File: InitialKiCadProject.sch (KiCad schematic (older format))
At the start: 0 parts

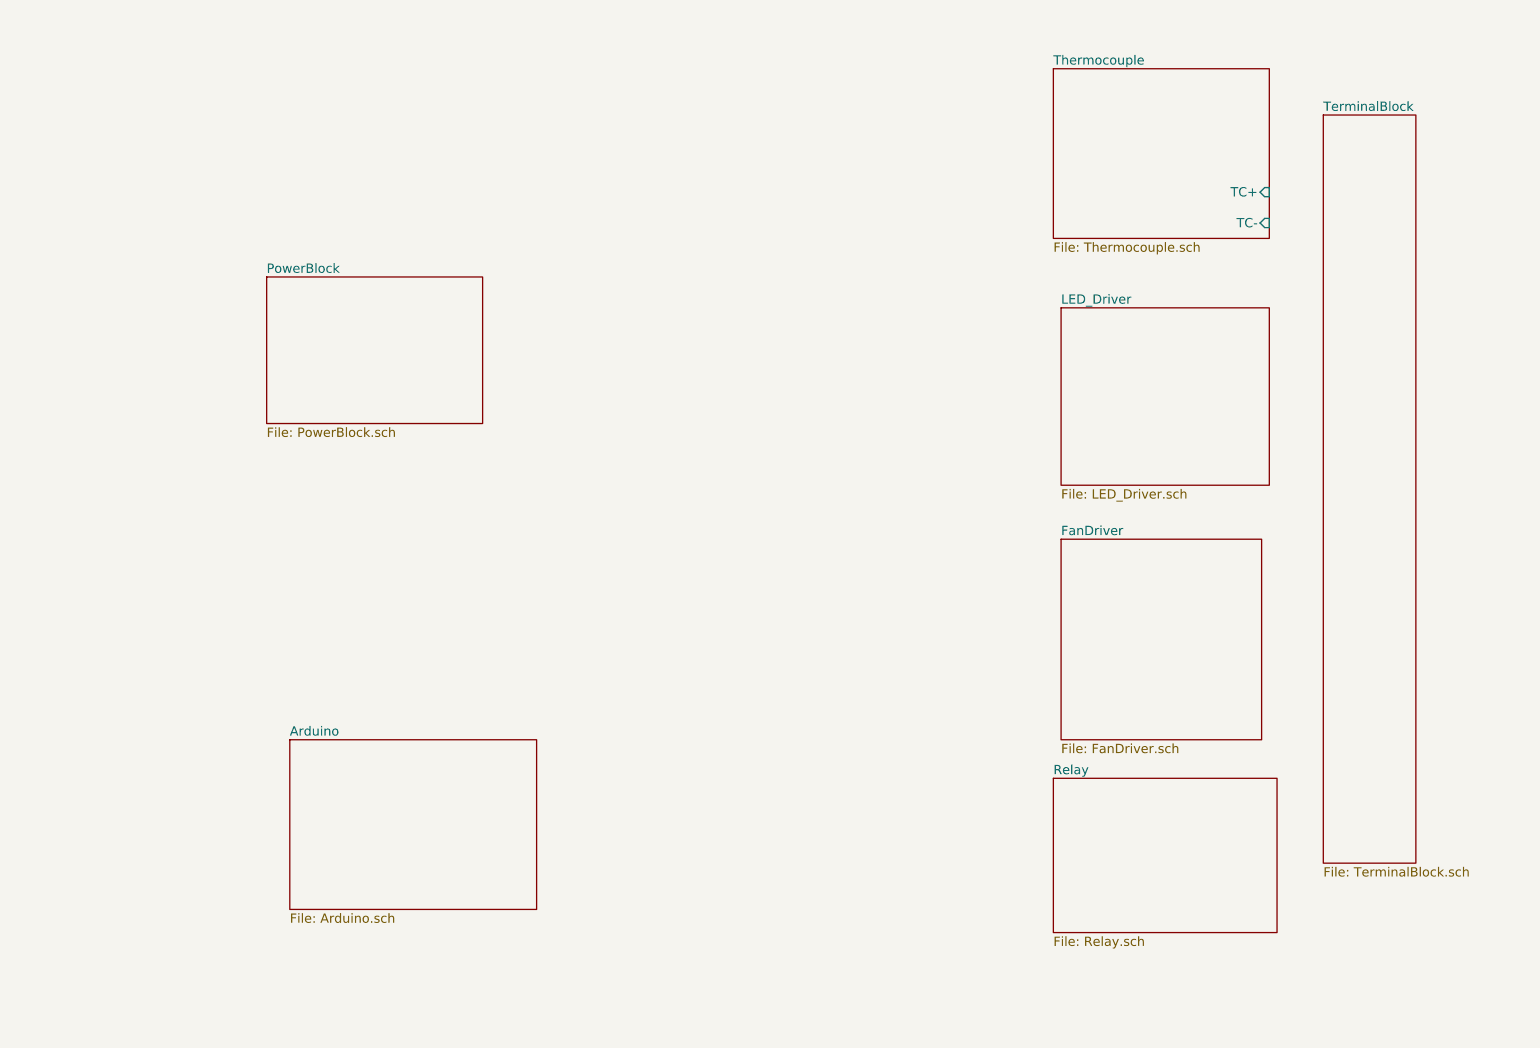
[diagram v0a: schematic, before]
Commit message: Added pins to sheets of block diagram.
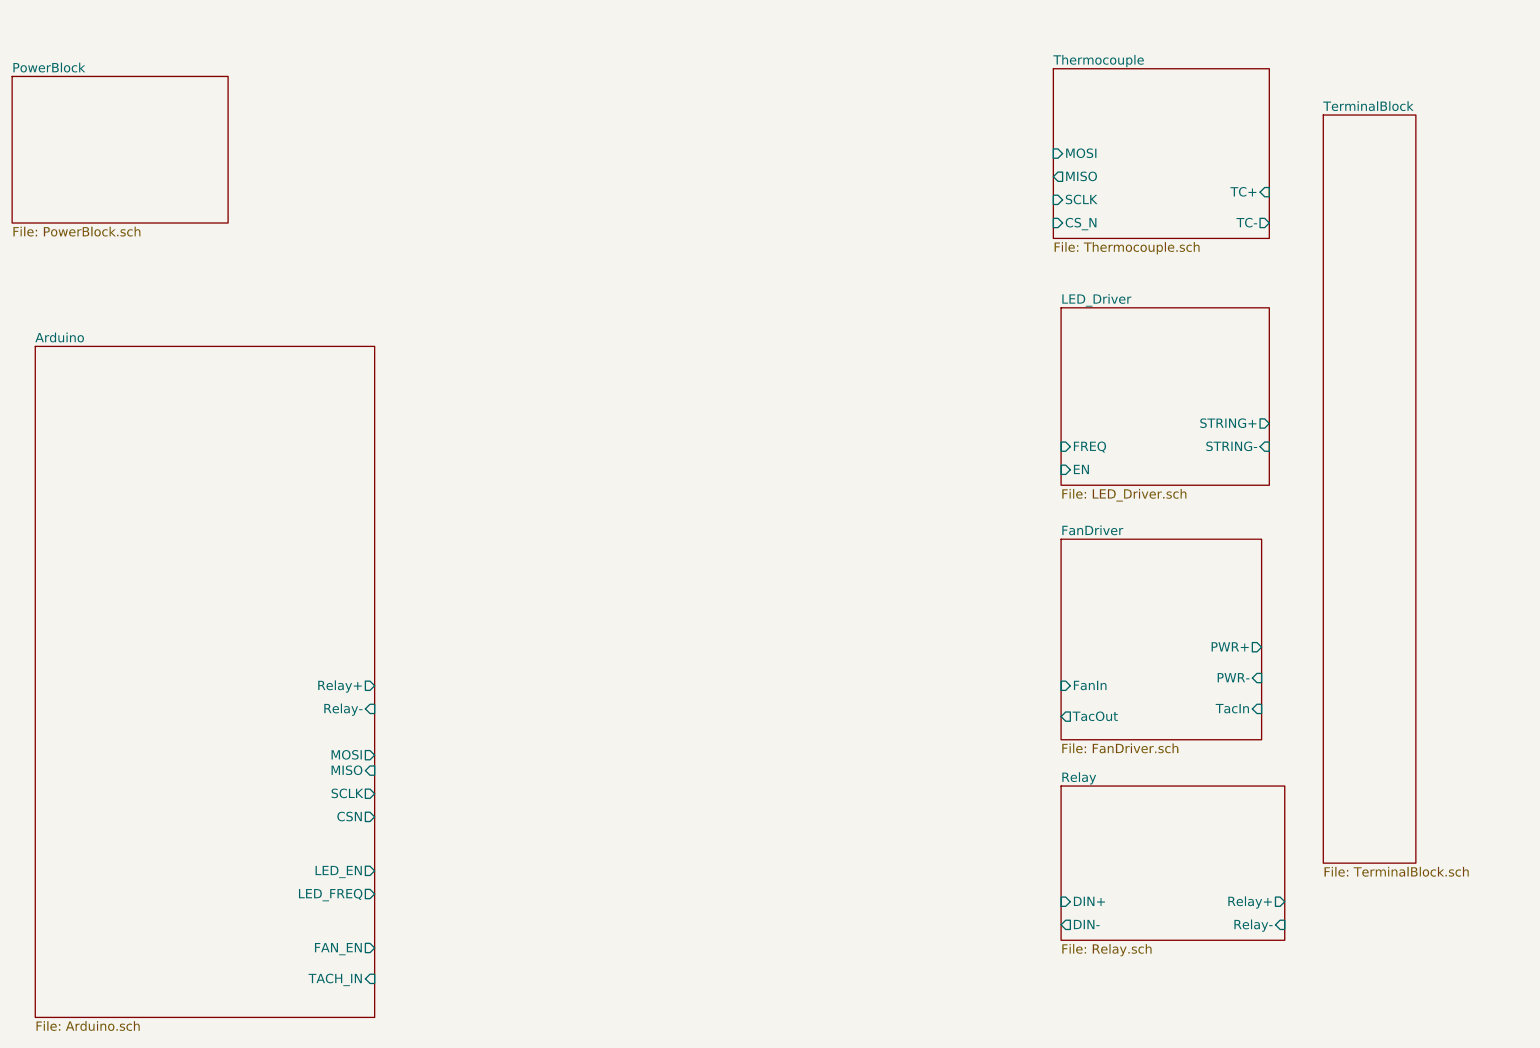
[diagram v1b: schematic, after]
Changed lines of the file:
@@
-EESchema Schematic File Version 2  date Tue 04 Feb 2014 11:04:27 PM EST
+EESchema Schematic File Version 2  date Tue 04 Feb 2014 11:45:57 PM EST
 LIBS:power
 LIBS:device
@@
 F0 "LED_Driver" 60
 F1 "LED_Driver.sch" 60
+F2 "STRING-" I R 9850 3600 60
+F3 "STRING+" O R 9850 3450 60
+F4 "FREQ" I L 8500 3600 60
+F5 "EN" I L 8500 3750 60
 $EndSheet
 $Sheet
@@
 F0 "FanDriver" 60
 F1 "FanDriver.sch" 60
+F2 "FanIn" I L 8500 5150 60
+F3 "TacOut" O L 8500 5350 60
+F4 "TacIn" I R 9800 5300 60
+F5 "PWR-" I R 9800 5100 60
+F6 "PWR+" O R 9800 4900 60
 $EndSheet
 $Sheet
-S 3350 2500 1400 950
+S 1700 1200 1400 950
 U 52F1B680
 F0 "PowerBlock" 60
@@
 $EndSheet
 $Sheet
-S 8450 5750 1450 1000
+S 8500 5800 1450 1000
 U 52F1B673
 F0 "Relay" 60
 F1 "Relay.sch" 60
+F2 "Relay-" I R 9950 6700 60
+F3 "Relay+" O R 9950 6550 60
+F4 "DIN-" O L 8500 6700 60
+F5 "DIN+" I L 8500 6550 60
 $EndSheet
 $Sheet
@@
 F0 "Thermocouple" 60
 F1 "Thermocouple.sch" 60
-F2 "TC-" I R 9850 2150 60
+F2 "TC-" O R 9850 2150 60
 F3 "TC+" I R 9850 1950 60
+F4 "CS_N" I L 8450 2150 60
+F5 "SCLK" I L 8450 2000 60
+F6 "MISO" O L 8450 1850 60
+F7 "MOSI" I L 8450 1700 60
 $EndSheet
 $Sheet
-S 3500 5500 1600 1100
+S 1850 2950 2200 4350
 U 52F1B5F2
 F0 "Arduino" 60
 F1 "Arduino.sch" 60
+F2 "TACH_IN" I R 4050 7050 60
+F3 "FAN_EN" O R 4050 6850 60
+F4 "LED_FREQ" O R 4050 6500 60
+F5 "LED_EN" O R 4050 6350 60
+F6 "CSN" O R 4050 6000 60
+F7 "SCLK" O R 4050 5850 60
+F8 "MISO" I R 4050 5700 60
+F9 "MOSI" O R 4050 5600 60
+F10 "Relay-" I R 4050 5300 60
+F11 "Relay+" O R 4050 5150 60
 $EndSheet
 $EndSCHEMATC

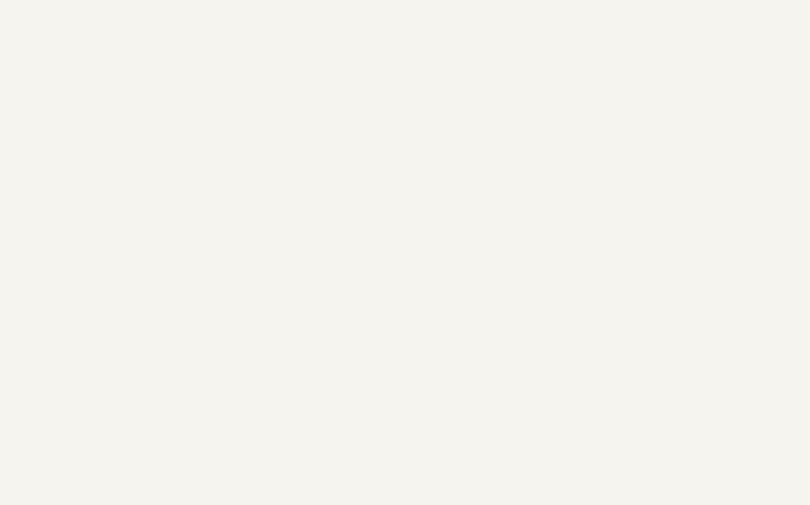
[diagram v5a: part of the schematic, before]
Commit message: added filter power section
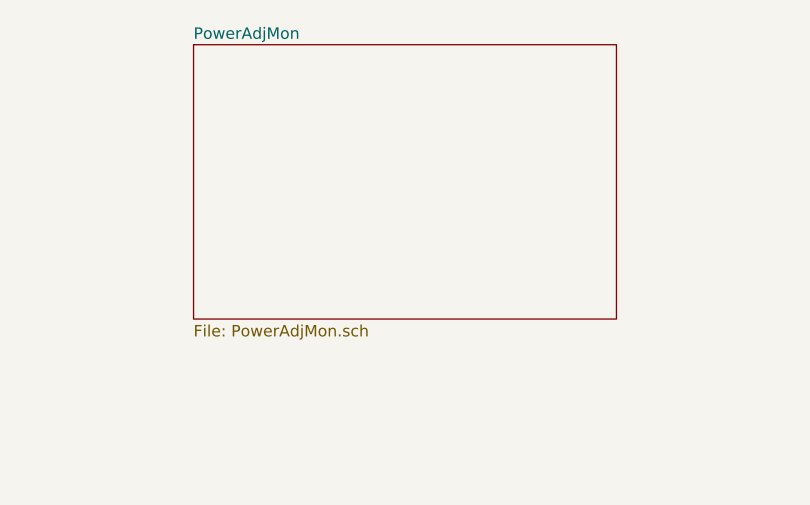
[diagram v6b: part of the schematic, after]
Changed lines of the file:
@@
 LIBS:arduino_shieldsNCL
 LIBS:spdt
+LIBS:BenchLib
 LIBS:InitialKiCadProject-cache
 EELAYER 27 0
@@
 $Descr A4 11693 8268
 encoding utf-8
-Sheet 1 8
+Sheet 1 9
 Title ""
 Date "7 feb 2014"
@@
 F11 "Relay+" O R 4050 5150 60
 $EndSheet
+$Sheet
+S 5000 1150 1850 1200
+U 52F452FD
+F0 "PowerAdjMon" 50
+F1 "PowerAdjMon.sch" 50
+$EndSheet
 $EndSCHEMATC

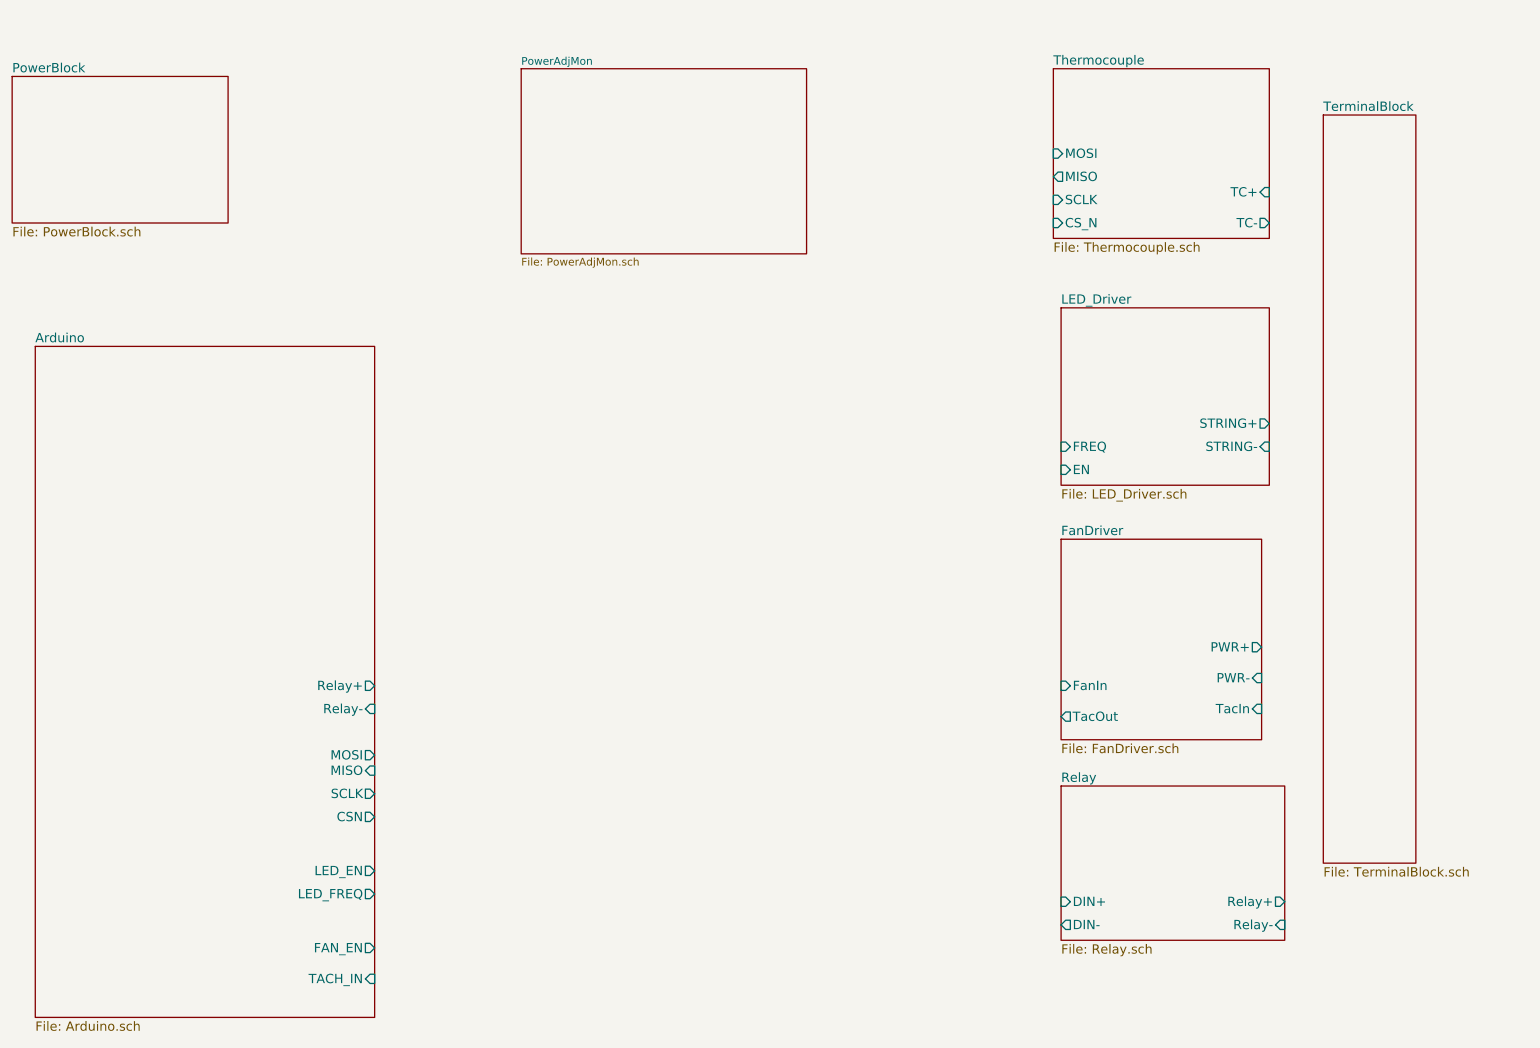
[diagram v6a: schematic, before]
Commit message: Added contents to Power Supply and monitor block
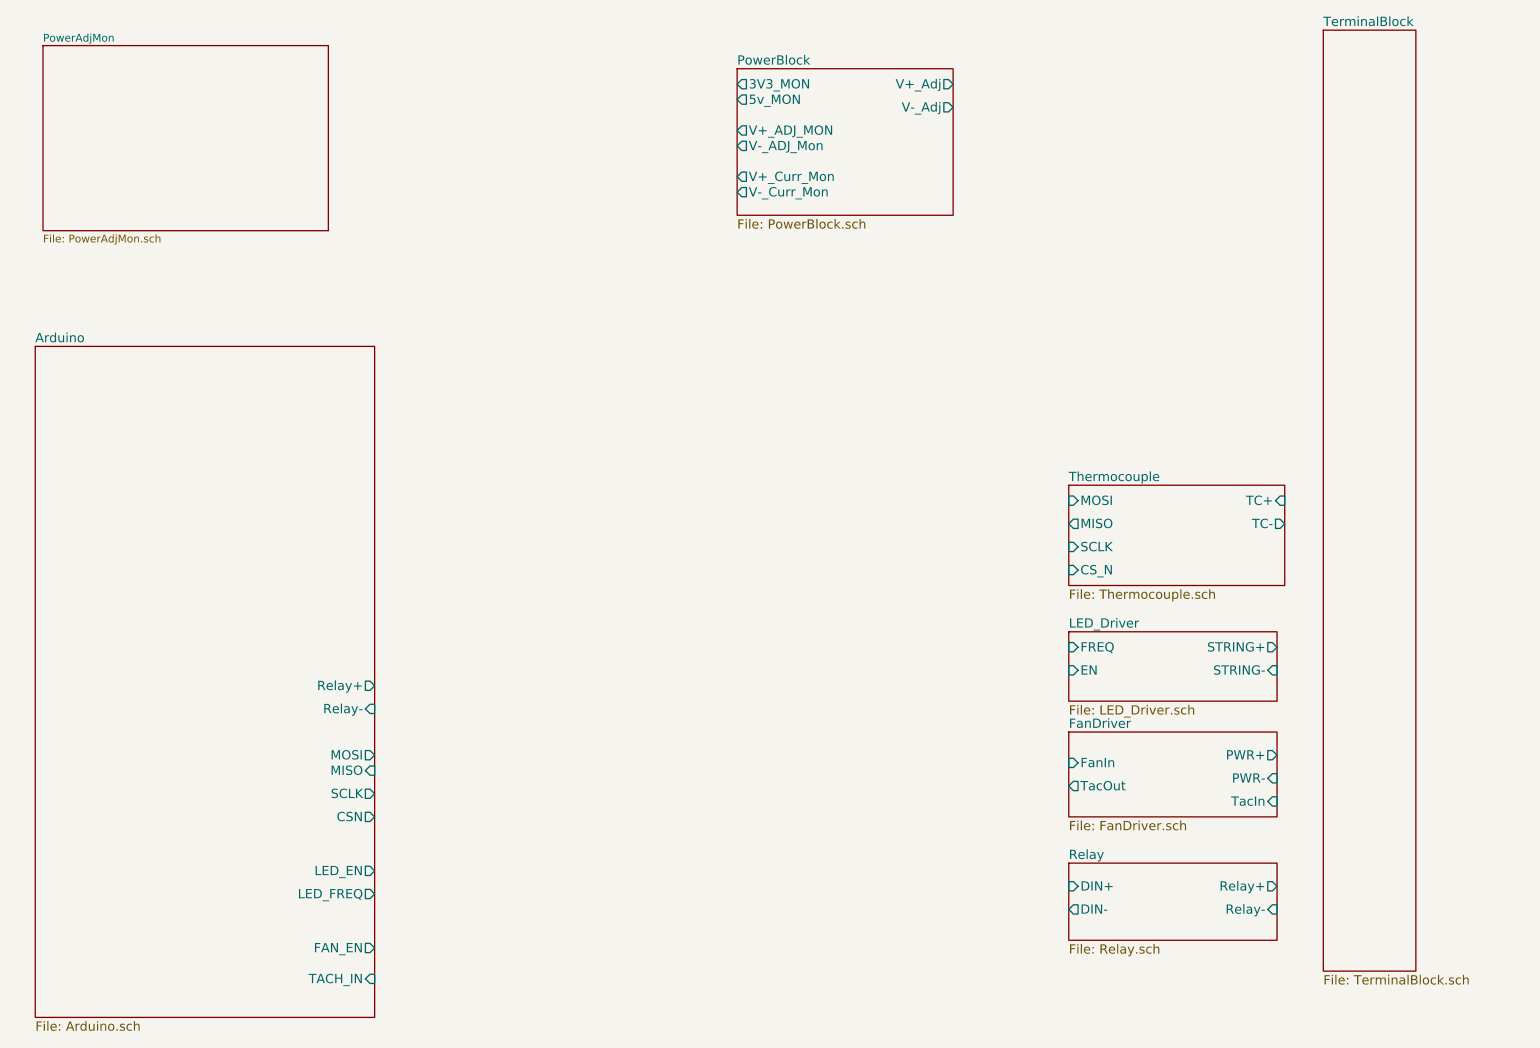
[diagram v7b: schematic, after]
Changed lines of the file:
@@
-EESchema Schematic File Version 2
+EESchema Schematic File Version 2  date Sat 08 Feb 2014 08:25:16 PM EST
 LIBS:power
 LIBS:device
@@
 LIBS:contrib
 LIBS:valves
-LIBS:arduino_shieldsNCL
 LIBS:spdt
 LIBS:BenchLib
 LIBS:InitialKiCadProject-cache
-EELAYER 27 0
+EELAYER 25  0
 EELAYER END
-$Descr A4 11693 8268
+$Descr A4 11700 8267
 encoding utf-8
 Sheet 1 9
 Title ""
-Date "7 feb 2014"
+Date "9 feb 2014"
 Rev ""
 Comp ""
@@
 $EndDescr
 $Sheet
-S 10200 1450 600  4850
+S 8550 4800 1350 450
+U 52F1B6CE
+F0 "LED_Driver" 60
+F1 "LED_Driver.sch" 60
+F2 "STRING-" I R 9900 5050 60
+F3 "STRING+" O R 9900 4900 60
+F4 "FREQ" I L 8550 4900 60
+F5 "EN" I L 8550 5050 60
+$EndSheet
+$Sheet
+S 10200 900  600  6100
 U 52F1B712
 F0 "TerminalBlock" 60
@@
 $EndSheet
 $Sheet
-S 8500 2700 1350 1150
-U 52F1B6CE
-F0 "LED_Driver" 60
-F1 "LED_Driver.sch" 60
-F2 "STRING-" I R 9850 3600 60
-F3 "STRING+" O R 9850 3450 60
-F4 "FREQ" I L 8500 3600 60
-F5 "EN" I L 8500 3750 60
-$EndSheet
-$Sheet
-S 8500 4200 1300 1300
+S 8550 5450 1350 550
 U 52F1B6C1
 F0 "FanDriver" 60
 F1 "FanDriver.sch" 60
-F2 "FanIn" I L 8500 5150 60
-F3 "TacOut" O L 8500 5350 60
-F4 "TacIn" I R 9800 5300 60
-F5 "PWR-" I R 9800 5100 60
-F6 "PWR+" O R 9800 4900 60
+F2 "FanIn" I L 8550 5650 60
+F3 "TacOut" O L 8550 5800 60
+F4 "TacIn" I R 9900 5900 60
+F5 "PWR-" I R 9900 5750 60
+F6 "PWR+" O R 9900 5600 60
 $EndSheet
 $Sheet
-S 1700 1200 1400 950
+S 6400 1150 1400 950
 U 52F1B680
 F0 "PowerBlock" 60
 F1 "PowerBlock.sch" 60
+F2 "V+_Curr_Mon" O L 6400 1850 60
+F3 "V-_Curr_Mon" O L 6400 1950 60
+F4 "V-_ADJ_Mon" O L 6400 1650 60
+F5 "V+_ADJ_MON" O L 6400 1550 60
+F6 "5v_MON" O L 6400 1350 60
+F7 "3V3_MON" O L 6400 1250 60
+F8 "V-_Adj" O R 7800 1400 60
+F9 "V+_Adj" O R 7800 1250 60
 $EndSheet
 $Sheet
-S 8500 5800 1450 1000
+S 8550 6300 1350 500
 U 52F1B673
 F0 "Relay" 60
 F1 "Relay.sch" 60
-F2 "Relay-" I R 9950 6700 60
-F3 "Relay+" O R 9950 6550 60
-F4 "DIN-" O L 8500 6700 60
-F5 "DIN+" I L 8500 6550 60
+F2 "Relay-" I R 9900 6600 60
+F3 "Relay+" O R 9900 6450 60
+F4 "DIN-" O L 8550 6600 60
+F5 "DIN+" I L 8550 6450 60
 $EndSheet
 $Sheet
-S 8450 1150 1400 1100
+S 8550 3850 1400 650
 U 52F1B638
 F0 "Thermocouple" 60
 F1 "Thermocouple.sch" 60
-F2 "TC-" O R 9850 2150 60
-F3 "TC+" I R 9850 1950 60
-F4 "CS_N" I L 8450 2150 60
-F5 "SCLK" I L 8450 2000 60
-F6 "MISO" O L 8450 1850 60
-F7 "MOSI" I L 8450 1700 60
+F2 "TC-" O R 9950 4100 60
+F3 "TC+" I R 9950 3950 60
+F4 "CS_N" I L 8550 4400 60
+F5 "SCLK" I L 8550 4250 60
+F6 "MISO" O L 8550 4100 60
+F7 "MOSI" I L 8550 3950 60
 $EndSheet
 $Sheet
@@
 $EndSheet
 $Sheet
-S 5000 1150 1850 1200
+S 1900 1000 1850 1200
 U 52F452FD
 F0 "PowerAdjMon" 50
